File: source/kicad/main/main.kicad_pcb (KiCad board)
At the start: 4 copper layers, 50 x 50 mm, 108 parts

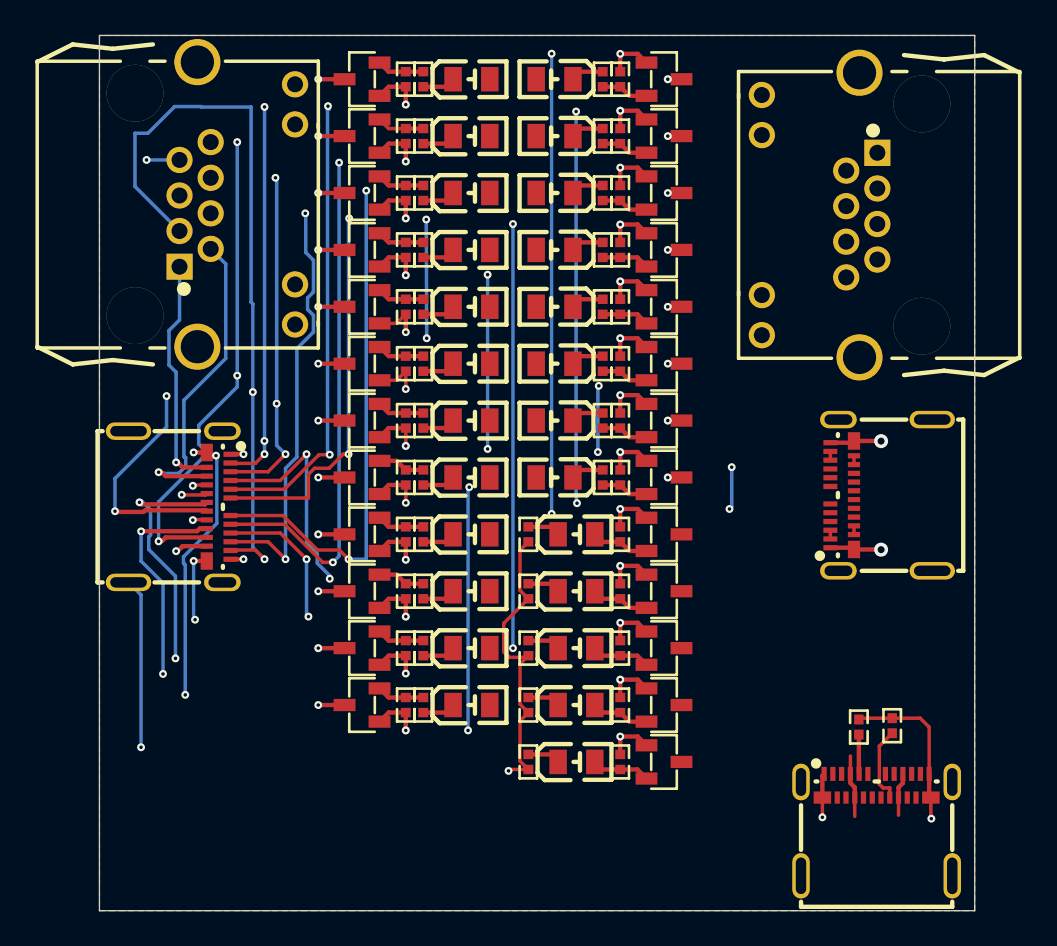
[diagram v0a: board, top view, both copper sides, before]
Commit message: bugfix/1.0.0 fixes (#3)
* Bugfixes 1.0.0; WIP; Not exported yet.

- Fixed USB-C PD resistors
- Improved part-picking
- Fixed LedIndicator (wrong PowerSwitch usage)
- Reduced LED brightness

* Fix footprints/3dmodels

* Place labels
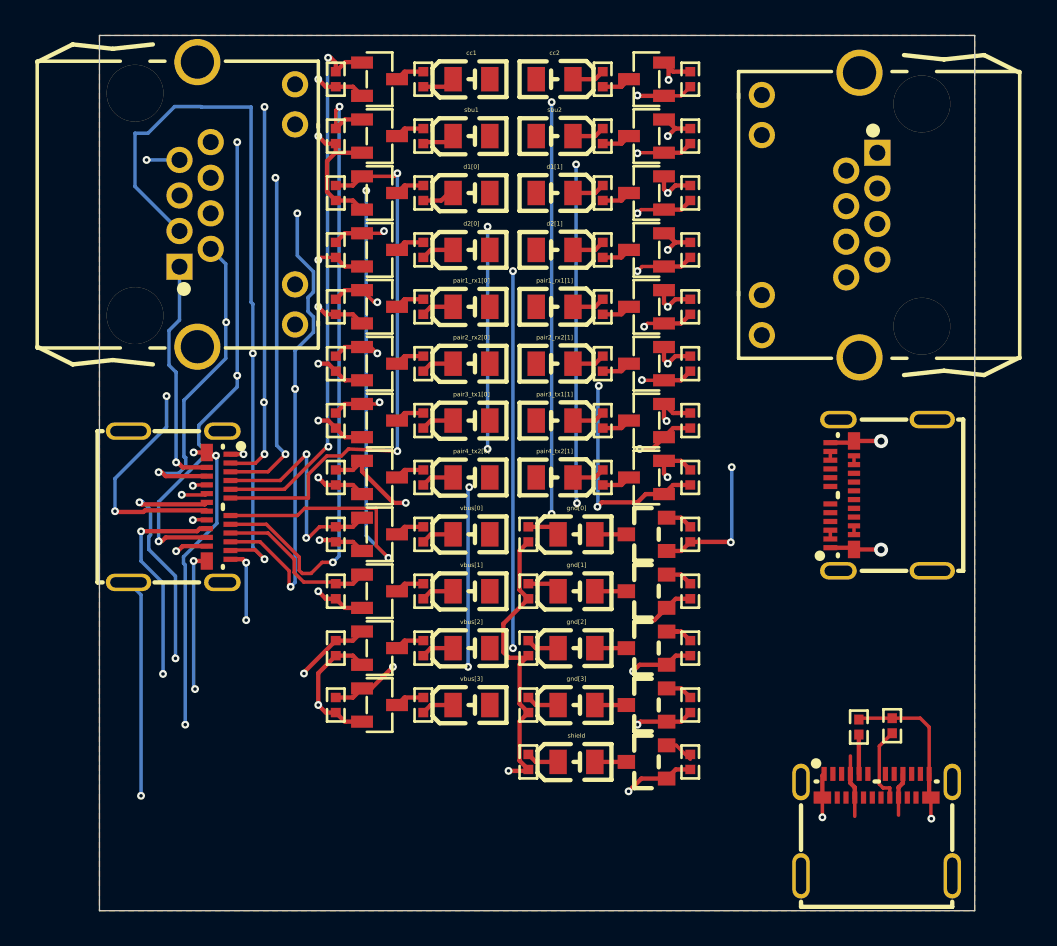
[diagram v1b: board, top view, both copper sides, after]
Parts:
- removed tester.cc1.indicator.led.current_limiting_resistor[Resistor:300Ω], tester.cc2.indicator.led.current_limiting_resistor[Resistor:300Ω], tester.d1[0].indicator.led.current_limiting_resistor[Resistor:300Ω], tester.d1[1].indicator.led.current_limiting_resistor[Resistor:300Ω], tester.d2[0].indicator.led.current_limiting_resistor[Resistor:300Ω], tester.d2[1].indicator.led.current_limiting_resistor[Resistor:300Ω], tester.gnd[0].indicator.led.current_limiting_resistor[Resistor:300Ω], tester.gnd[1].indicator.led.current_limiting_resistor[Resistor:300Ω], tester.gnd[2].indicator.led.current_limiting_resistor[Resistor:300Ω], tester.gnd[3].indicator.led.current_limiting_resistor[Resistor:300Ω], tester.pair1_rx1[0].indicator.led.current_limiting_resistor[Resistor:300Ω], tester.pair1_rx1[1].indicator.led.current_limiting_resistor[Resistor:300Ω], tester.pair2_rx2[0].indicator.led.current_limiting_resistor[Resistor:300Ω], tester.pair2_rx2[1].indicator.led.current_limiting_resistor[Resistor:300Ω], tester.pair3_tx1[0].indicator.led.current_limiting_resistor[Resistor:300Ω], tester.pair3_tx1[1].indicator.led.current_limiting_resistor[Resistor:300Ω], tester.pair4_tx2[0].indicator.led.current_limiting_resistor[Resistor:300Ω], tester.pair4_tx2[1].indicator.led.current_limiting_resistor[Resistor:300Ω], tester.sbu1.indicator.led.current_limiting_resistor[Resistor:300Ω], tester.sbu2.indicator.led.current_limiting_resistor[Resistor:300Ω], tester.shield.indicator.led.current_limiting_resistor[Resistor:300Ω], tester.vbus[0].indicator.led.current_limiting_resistor[Resistor:300Ω], tester.vbus[1].indicator.led.current_limiting_resistor[Resistor:300Ω], tester.vbus[2].indicator.led.current_limiting_resistor[Resistor:300Ω], tester.vbus[3].indicator.led.current_limiting_resistor[Resistor:300Ω]: 300Ω, lcsc:R0402
- removed the tester.gnd[0].indicator.power_switch.mosfet[MOSFET:Q] at (32.2, 28.5)
- removed the tester.gnd[1].indicator.power_switch.mosfet[MOSFET:Q] at (32.2, 31.8)
- removed the tester.gnd[2].indicator.power_switch.mosfet[MOSFET:Q] at (32.2, 35.0)
- removed the tester.gnd[3].indicator.power_switch.mosfet[MOSFET:Q] at (32.2, 38.2)
- removed the tester.shield.indicator.power_switch.mosfet[MOSFET:Q] at (32.2, 41.5)
- added tester.cc1.indicator.led.current_limiting_resistor[Resistor:1KΩ]: 1KΩ, lcsc:R0402, F.Cu at (18.5, 2.50)
- added tester.cc2.indicator.led.current_limiting_resistor[Resistor:1KΩ]: 1KΩ, lcsc:R0402, F.Cu at (28.8, 2.50)
- added tester.d1[0].indicator.led.current_limiting_resistor[Resistor:1KΩ]: 1KΩ, lcsc:R0402, F.Cu at (18.5, 9.00)
- added tester.d1[1].indicator.led.current_limiting_resistor[Resistor:1KΩ]: 1KΩ, lcsc:R0402, F.Cu at (28.8, 9.00)
- added tester.d2[0].indicator.led.current_limiting_resistor[Resistor:1KΩ]: 1KΩ, lcsc:R0402, F.Cu at (18.5, 12.2)
- added tester.d2[1].indicator.led.current_limiting_resistor[Resistor:1KΩ]: 1KΩ, lcsc:R0402, F.Cu at (28.8, 12.2)
- added tester.gnd[0].indicator.led.current_limiting_resistor[Resistor:1KΩ]: 1KΩ, lcsc:R0402, F.Cu at (24.5, 28.5)
- added tester.gnd[0].indicator.power_switch.mosfet[MOSFET:Q]: Q, lcsc:SOT-23_L2.9-W1.3-P1.90-LS2.4-BR, F.Cu at (31.2, 28.5)
- added tester.gnd[1].indicator.led.current_limiting_resistor[Resistor:1KΩ]: 1KΩ, lcsc:R0402, F.Cu at (24.5, 31.8)
- added tester.gnd[1].indicator.power_switch.mosfet[MOSFET:Q]: Q, lcsc:SOT-23_L2.9-W1.3-P1.90-LS2.4-BR, F.Cu at (31.2, 31.8)
- added tester.gnd[2].indicator.led.current_limiting_resistor[Resistor:1KΩ]: 1KΩ, lcsc:R0402, F.Cu at (24.5, 35.0)
- added tester.gnd[2].indicator.power_switch.mosfet[MOSFET:Q]: Q, lcsc:SOT-23_L2.9-W1.3-P1.90-LS2.4-BR, F.Cu at (31.2, 35.0)
- added tester.gnd[3].indicator.led.current_limiting_resistor[Resistor:1KΩ]: 1KΩ, lcsc:R0402, F.Cu at (24.5, 38.2)
- added tester.gnd[3].indicator.power_switch.mosfet[MOSFET:Q]: Q, lcsc:SOT-23_L2.9-W1.3-P1.90-LS2.4-BR, F.Cu at (31.2, 38.2)
- added tester.pair1_rx1[0].indicator.led.current_limiting_resistor[Resistor:1KΩ]: 1KΩ, lcsc:R0402, F.Cu at (18.5, 15.5)
- added tester.pair1_rx1[1].indicator.led.current_limiting_resistor[Resistor:1KΩ]: 1KΩ, lcsc:R0402, F.Cu at (28.8, 15.5)
- added tester.pair2_rx2[0].indicator.led.current_limiting_resistor[Resistor:1KΩ]: 1KΩ, lcsc:R0402, F.Cu at (18.5, 18.8)
- added tester.pair2_rx2[1].indicator.led.current_limiting_resistor[Resistor:1KΩ]: 1KΩ, lcsc:R0402, F.Cu at (28.8, 18.8)
- added tester.pair3_tx1[0].indicator.led.current_limiting_resistor[Resistor:1KΩ]: 1KΩ, lcsc:R0402, F.Cu at (18.5, 22.0)
- added tester.pair3_tx1[1].indicator.led.current_limiting_resistor[Resistor:1KΩ]: 1KΩ, lcsc:R0402, F.Cu at (28.8, 22.0)
- added tester.pair4_tx2[0].indicator.led.current_limiting_resistor[Resistor:1KΩ]: 1KΩ, lcsc:R0402, F.Cu at (18.5, 25.2)
- added tester.pair4_tx2[1].indicator.led.current_limiting_resistor[Resistor:1KΩ]: 1KΩ, lcsc:R0402, F.Cu at (28.8, 25.2)
- added tester.sbu1.indicator.led.current_limiting_resistor[Resistor:1KΩ]: 1KΩ, lcsc:R0402, F.Cu at (18.5, 5.75)
- added tester.sbu2.indicator.led.current_limiting_resistor[Resistor:1KΩ]: 1KΩ, lcsc:R0402, F.Cu at (28.8, 5.75)
- added tester.shield.indicator.led.current_limiting_resistor[Resistor:1KΩ]: 1KΩ, lcsc:R0402, F.Cu at (24.5, 41.5)
- added tester.shield.indicator.power_switch.mosfet[MOSFET:Q]: Q, lcsc:SOT-23_L2.9-W1.3-P1.90-LS2.4-BR, F.Cu at (31.2, 41.5)
- added tester.vbus[0].indicator.led.current_limiting_resistor[Resistor:1KΩ]: 1KΩ, lcsc:R0402, F.Cu at (18.5, 28.5)
- added tester.vbus[1].indicator.led.current_limiting_resistor[Resistor:1KΩ]: 1KΩ, lcsc:R0402, F.Cu at (18.5, 31.8)
- added tester.vbus[2].indicator.led.current_limiting_resistor[Resistor:1KΩ]: 1KΩ, lcsc:R0402, F.Cu at (18.5, 35.0)
- added tester.vbus[3].indicator.led.current_limiting_resistor[Resistor:1KΩ]: 1KΩ, lcsc:R0402, F.Cu at (18.5, 38.2)
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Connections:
- net psu.configuration_resistors[0][Resistor:5.0KΩ]-psu.usb[USB_C_Receptacle:x] renamed psu.usb[USB_C_Receptacle:x]-psu.configuration_resistors[0][Resistor:5.0KΩ]
- net tester.cc1[PairTester:virt]:4-tester.cc1.indicator[LEDIndicator:virt]-tester.cc1.indicator.power_swi renamed tester.cc1.indicator[LEDIndicator:virt]-tester.cc1.indicator.power_switch[PowerSwitch:virt]-tester.c
- net tester.cc2[PairTester:virt]:4-tester.cc2.indicator.power_switch[PowerSwitch:virt]-tester.cc2.indicat renamed tester.cc2.indicator.power_switch[PowerSwitch:virt]-tester.cc2.indicator[LEDIndicator:virt]-tester.c
- net tester.d1[0].indicator.power_switch[PowerSwitch:virt]-tester.d1[0][PairTester:virt]:4-tester.d1[0].i renamed tester.d1[0].indicator[LEDIndicator:virt]-tester.d1[0].indicator.power_switch[PowerSwitch:virt]-test
- net tester.d1[1].indicator.power_switch[PowerSwitch:virt]-tester.d1[1].indicator[LEDIndicator:virt]-test renamed tester.d1[1].indicator.power_switch[PowerSwitch:virt]-tester.d1[1][PairTester:virt]:4-tester.d1[1].i
- net tester.d2[1].indicator.power_switch[PowerSwitch:virt]-tester.d2[1][PairTester:virt]:4-tester.d2[1].i renamed tester.d2[1][PairTester:virt]:4-tester.d2[1].indicator[LEDIndicator:virt]-tester.d2[1].indicator.pow
- net tester.gnd[0].indicator[LEDIndicator:virt]-tester.gnd[0][PairTester:virt]:4-tester.gnd[0].indicator. renamed tester.gnd[0].indicator.power_switch[PowerSwitch:virt]-tester.gnd[0].indicator[LEDIndicator:virt]-te
- net tester.gnd[1].indicator[LEDIndicator:virt]-tester.gnd[1][PairTester:virt]:4-tester.gnd[1].indicator. renamed tester.gnd[1][PairTester:virt]:4-tester.gnd[1].indicator.power_switch[PowerSwitch:virt]-tester.gnd[1
- net tester.gnd[2].indicator[LEDIndicator:virt]-tester.gnd[2][PairTester:virt]:4-tester.gnd[2].indicator. renamed tester.gnd[2][PairTester:virt]:4-tester.gnd[2].indicator[LEDIndicator:virt]-tester.gnd[2].indicator.
- net tester.pair1_rx1[0].indicator[LEDIndicator:virt]-tester.pair1_rx1[0][PairTester:virt]:4-tester.pair1 renamed tester.pair1_rx1[0][PairTester:virt]:4-tester.pair1_rx1[0].indicator.power_switch[PowerSwitch:virt]-
- net tester.pair1_rx1[1][PairTester:virt]:4-tester.pair1_rx1[1].indicator.power_switch[PowerSwitch:virt]- renamed tester.pair1_rx1[1][PairTester:virt]:4-tester.pair1_rx1[1].indicator[LEDIndicator:virt]-tester.pair1
- net tester.pair2_rx2[0].indicator.power_switch[PowerSwitch:virt]-tester.pair2_rx2[0].indicator[LEDIndica renamed tester.pair2_rx2[0].indicator[LEDIndicator:virt]-tester.pair2_rx2[0][PairTester:virt]:4-tester.pair2
- net tester.pair2_rx2[1].indicator[LEDIndicator:virt]-tester.pair2_rx2[1][PairTester:virt]:4-tester.pair2 renamed tester.pair2_rx2[1].indicator.power_switch[PowerSwitch:virt]-tester.pair2_rx2[1].indicator[LEDIndica
- net tester.pair3_tx1[0].indicator[LEDIndicator:virt]-tester.pair3_tx1[0][PairTester:virt]:4-tester.pair3 renamed tester.pair3_tx1[0].indicator.power_switch[PowerSwitch:virt]-tester.pair3_tx1[0][PairTester:virt]:4-
- net tester.pair4_tx2[0].indicator.power_switch[PowerSwitch:virt]-tester.pair4_tx2[0].indicator[LEDIndica renamed tester.pair4_tx2[0].indicator[LEDIndicator:virt]-tester.pair4_tx2[0].indicator.power_switch[PowerSwi
- net tester.pair4_tx2[1][PairTester:virt]:4-tester.pair4_tx2[1].indicator[LEDIndicator:virt]-tester.pair4 renamed tester.pair4_tx2[1].indicator[LEDIndicator:virt]-tester.pair4_tx2[1].indicator.power_switch[PowerSwi
- net tester.sbu2[PairTester:virt]:4-tester.sbu2.indicator.power_switch[PowerSwitch:virt]-tester.sbu2.indi renamed tester.sbu2.indicator.power_switch[PowerSwitch:virt]-tester.sbu2[PairTester:virt]:4-tester.sbu2.indi
- net tester.shield[PairTester:virt]:4-tester.shield.indicator[LEDIndicator:virt]-tester.shield.indicator. renamed tester.shield.indicator.power_switch[PowerSwitch:virt]-tester.shield.indicator[LEDIndicator:virt]-te
- net tester.vbus[0].indicator[LEDIndicator:virt]-tester.vbus[0][PairTester:virt]:4-tester.vbus[0].indicat renamed tester.vbus[0][PairTester:virt]:4-tester.vbus[0].indicator[LEDIndicator:virt]-tester.vbus[0].indicat
- net tester.vbus[1].indicator.power_switch[PowerSwitch:virt]-tester.vbus[1][PairTester:virt]:4-tester.vbu renamed tester.vbus[1][PairTester:virt]:4-tester.vbus[1].indicator.power_switch[PowerSwitch:virt]-tester.vbu
- psu.configuration_resistors[0][Resistor:5.0KΩ] pad 2: tester.pair1_rx1[1][PairTester:virt]:2-tester.cc1[PairTester:virt]:2-tester.gnd[0].indicator.power_s -> tester.vbus[1].indicator[LEDIndicator:virt]:3-tester.shield.indicator[LEDIndicator:virt]:3-tester.gn
- psu.configuration_resistors[1][Resistor:5.0KΩ] pad 2: tester.pair1_rx1[1][PairTester:virt]:2-tester.cc1[PairTester:virt]:2-tester.gnd[0].indicator.power_s -> tester.vbus[1].indicator[LEDIndicator:virt]:3-tester.shield.indicator[LEDIndicator:virt]:3-tester.gn
- psu.usb[USB_C_Receptacle:x] pad A1: tester.pair1_rx1[1][PairTester:virt]:2-tester.cc1[PairTester:virt]:2-tester.gnd[0].indicator.power_s -> tester.vbus[1].indicator[LEDIndicator:virt]:3-tester.shield.indicator[LEDIndicator:virt]:3-tester.gn
- psu.usb[USB_C_Receptacle:x] pad A12: tester.pair1_rx1[1][PairTester:virt]:2-tester.cc1[PairTester:virt]:2-tester.gnd[0].indicator.power_s -> tester.vbus[1].indicator[LEDIndicator:virt]:3-tester.shield.indicator[LEDIndicator:virt]:3-tester.gn
- psu.usb[USB_C_Receptacle:x] pad A4: tester.d1[1].indicator.power_switch[PowerSwitch:virt]:4-tester.pair1_rx1[0].indicator.power_switch[P -> tester.pair1_rx1[1].indicator.led[PoweredLED:virt]-tester.d2[1].indicator.power_switch[PowerSwitch:v
- psu.usb[USB_C_Receptacle:x] pad A9: tester.d1[1].indicator.power_switch[PowerSwitch:virt]:4-tester.pair1_rx1[0].indicator.power_switch[P -> tester.pair1_rx1[1].indicator.led[PoweredLED:virt]-tester.d2[1].indicator.power_switch[PowerSwitch:v
- psu.usb[USB_C_Receptacle:x] pad B1: tester.pair1_rx1[1][PairTester:virt]:2-tester.cc1[PairTester:virt]:2-tester.gnd[0].indicator.power_s -> tester.vbus[1].indicator[LEDIndicator:virt]:3-tester.shield.indicator[LEDIndicator:virt]:3-tester.gn
- psu.usb[USB_C_Receptacle:x] pad B12: tester.pair1_rx1[1][PairTester:virt]:2-tester.cc1[PairTester:virt]:2-tester.gnd[0].indicator.power_s -> tester.vbus[1].indicator[LEDIndicator:virt]:3-tester.shield.indicator[LEDIndicator:virt]:3-tester.gn
- psu.usb[USB_C_Receptacle:x] pad B4: tester.d1[1].indicator.power_switch[PowerSwitch:virt]:4-tester.pair1_rx1[0].indicator.power_switch[P -> tester.pair1_rx1[1].indicator.led[PoweredLED:virt]-tester.d2[1].indicator.power_switch[PowerSwitch:v
- psu.usb[USB_C_Receptacle:x] pad B9: tester.d1[1].indicator.power_switch[PowerSwitch:virt]:4-tester.pair1_rx1[0].indicator.power_switch[P -> tester.pair1_rx1[1].indicator.led[PoweredLED:virt]-tester.d2[1].indicator.power_switch[PowerSwitch:v
- tester.cc1.indicator.led.led[LED:D] pad 1: tester.d1[1].indicator.power_switch[PowerSwitch:virt]:4-tester.pair1_rx1[0].indicator.power_switch[P -> tester.pair1_rx1[1].indicator.led[PoweredLED:virt]-tester.d2[1].indicator.power_switch[PowerSwitch:v
- tester.cc1.indicator.led.led[LED:D] pad 2: tester.cc1.indicator.led.led[LED:D]-tester.cc1.indicator.led.current_limiting_resistor[Resistor:300Ω] -> tester.cc1.indicator.led.current_limiting_resistor[Resistor:1KΩ]-tester.cc1.indicator.led.led[LED:D]
- tester.cc1.indicator.power_switch.mosfet[MOSFET:Q] pad 2: tester.cc1.indicator.led[PoweredLED:virt]:2-tester.cc1.indicator.power_switch[PowerSwitch:virt]:3 -> tester.vbus[1].indicator[LEDIndicator:virt]:3-tester.shield.indicator[LEDIndicator:virt]:3-tester.gn
- tester.cc1.indicator.power_switch.mosfet[MOSFET:Q] pad 3: tester.pair1_rx1[1][PairTester:virt]:2-tester.cc1[PairTester:virt]:2-tester.gnd[0].indicator.power_s -> tester.cc1.indicator.power_switch[PowerSwitch:virt]:5-tester.cc1.indicator.led[PoweredLED:virt]:2
- tester.cc1.indicator.power_switch.pull_resistor[Resistor:100KΩ] pad 2: tester.cc1.indicator.led[PoweredLED:virt]:2-tester.cc1.indicator.power_switch[PowerSwitch:virt]:3 -> tester.vbus[1].indicator[LEDIndicator:virt]:3-tester.shield.indicator[LEDIndicator:virt]:3-tester.gn
- tester.cc2.indicator.led.led[LED:D] pad 1: tester.d1[1].indicator.power_switch[PowerSwitch:virt]:4-tester.pair1_rx1[0].indicator.power_switch[P -> tester.pair1_rx1[1].indicator.led[PoweredLED:virt]-tester.d2[1].indicator.power_switch[PowerSwitch:v
- tester.cc2.indicator.led.led[LED:D] pad 2: tester.cc2.indicator.led.current_limiting_resistor[Resistor:300Ω]-tester.cc2.indicator.led.led[LED:D] -> tester.cc2.indicator.led.led[LED:D]-tester.cc2.indicator.led.current_limiting_resistor[Resistor:1KΩ]
- tester.cc2.indicator.power_switch.mosfet[MOSFET:Q] pad 2: tester.cc2.indicator.power_switch[PowerSwitch:virt]:3-tester.cc2.indicator.led[PoweredLED:virt]:2 -> tester.vbus[1].indicator[LEDIndicator:virt]:3-tester.shield.indicator[LEDIndicator:virt]:3-tester.gn
- tester.cc2.indicator.power_switch.mosfet[MOSFET:Q] pad 3: tester.pair1_rx1[1][PairTester:virt]:2-tester.cc1[PairTester:virt]:2-tester.gnd[0].indicator.power_s -> tester.cc2.indicator.power_switch[PowerSwitch:virt]:5-tester.cc2.indicator.led[PoweredLED:virt]:2
- tester.cc2.indicator.power_switch.pull_resistor[Resistor:100KΩ] pad 2: tester.cc2.indicator.power_switch[PowerSwitch:virt]:3-tester.cc2.indicator.led[PoweredLED:virt]:2 -> tester.vbus[1].indicator[LEDIndicator:virt]:3-tester.shield.indicator[LEDIndicator:virt]:3-tester.gn
- tester.d1[0].indicator.led.led[LED:D] pad 1: tester.d1[1].indicator.power_switch[PowerSwitch:virt]:4-tester.pair1_rx1[0].indicator.power_switch[P -> tester.pair1_rx1[1].indicator.led[PoweredLED:virt]-tester.d2[1].indicator.power_switch[PowerSwitch:v
- tester.d1[0].indicator.led.led[LED:D] pad 2: tester.d1[0].indicator.led.led[LED:D]-tester.d1[0].indicator.led.current_limiting_resistor[Resistor:300Ω] -> tester.d1[0].indicator.led.current_limiting_resistor[Resistor:1KΩ]-tester.d1[0].indicator.led.led[LED:D]
- tester.d1[0].indicator.power_switch.mosfet[MOSFET:Q] pad 2: tester.d1[0].indicator.led[PoweredLED:virt]:2-tester.d1[0].indicator.power_switch[PowerSwitch:virt]: -> tester.vbus[1].indicator[LEDIndicator:virt]:3-tester.shield.indicator[LEDIndicator:virt]:3-tester.gn
- tester.d1[0].indicator.power_switch.mosfet[MOSFET:Q] pad 3: tester.pair1_rx1[1][PairTester:virt]:2-tester.cc1[PairTester:virt]:2-tester.gnd[0].indicator.power_s -> tester.d1[0].indicator.led[PoweredLED:virt]:2-tester.d1[0].indicator.power_switch[PowerSwitch:virt]:
- tester.d1[0].indicator.power_switch.pull_resistor[Resistor:100KΩ] pad 2: tester.d1[0].indicator.led[PoweredLED:virt]:2-tester.d1[0].indicator.power_switch[PowerSwitch:virt]: -> tester.vbus[1].indicator[LEDIndicator:virt]:3-tester.shield.indicator[LEDIndicator:virt]:3-tester.gn
- tester.d1[1].indicator.led.led[LED:D] pad 1: tester.d1[1].indicator.power_switch[PowerSwitch:virt]:4-tester.pair1_rx1[0].indicator.power_switch[P -> tester.pair1_rx1[1].indicator.led[PoweredLED:virt]-tester.d2[1].indicator.power_switch[PowerSwitch:v
- tester.d1[1].indicator.led.led[LED:D] pad 2: tester.d1[1].indicator.led.current_limiting_resistor[Resistor:300Ω]-tester.d1[1].indicator.led.led[LED:D] -> tester.d1[1].indicator.led.led[LED:D]-tester.d1[1].indicator.led.current_limiting_resistor[Resistor:1KΩ]
- tester.d1[1].indicator.power_switch.mosfet[MOSFET:Q] pad 2: tester.d1[1].indicator.led[PoweredLED:virt]:2-tester.d1[1].indicator.power_switch[PowerSwitch:virt]: -> tester.vbus[1].indicator[LEDIndicator:virt]:3-tester.shield.indicator[LEDIndicator:virt]:3-tester.gn
- tester.d1[1].indicator.power_switch.mosfet[MOSFET:Q] pad 3: tester.pair1_rx1[1][PairTester:virt]:2-tester.cc1[PairTester:virt]:2-tester.gnd[0].indicator.power_s -> tester.d1[1].indicator.power_switch[PowerSwitch:virt]:5-tester.d1[1].indicator.led[PoweredLED:virt]:
- tester.d1[1].indicator.power_switch.pull_resistor[Resistor:100KΩ] pad 2: tester.d1[1].indicator.led[PoweredLED:virt]:2-tester.d1[1].indicator.power_switch[PowerSwitch:virt]: -> tester.vbus[1].indicator[LEDIndicator:virt]:3-tester.shield.indicator[LEDIndicator:virt]:3-tester.gn
- tester.d2[0].indicator.led.led[LED:D] pad 1: tester.d1[1].indicator.power_switch[PowerSwitch:virt]:4-tester.pair1_rx1[0].indicator.power_switch[P -> tester.pair1_rx1[1].indicator.led[PoweredLED:virt]-tester.d2[1].indicator.power_switch[PowerSwitch:v
- tester.d2[0].indicator.led.led[LED:D] pad 2: tester.d2[0].indicator.led.current_limiting_resistor[Resistor:300Ω]-tester.d2[0].indicator.led.led[LED:D] -> tester.d2[0].indicator.led.current_limiting_resistor[Resistor:1KΩ]-tester.d2[0].indicator.led.led[LED:D]
- tester.d2[0].indicator.power_switch.mosfet[MOSFET:Q] pad 2: tester.d2[0].indicator.led[PoweredLED:virt]:2-tester.d2[0].indicator.power_switch[PowerSwitch:virt]: -> tester.vbus[1].indicator[LEDIndicator:virt]:3-tester.shield.indicator[LEDIndicator:virt]:3-tester.gn
- tester.d2[0].indicator.power_switch.mosfet[MOSFET:Q] pad 3: tester.pair1_rx1[1][PairTester:virt]:2-tester.cc1[PairTester:virt]:2-tester.gnd[0].indicator.power_s -> tester.d2[0].indicator.power_switch[PowerSwitch:virt]:5-tester.d2[0].indicator.led[PoweredLED:virt]:
- tester.d2[0].indicator.power_switch.pull_resistor[Resistor:100KΩ] pad 2: tester.d2[0].indicator.led[PoweredLED:virt]:2-tester.d2[0].indicator.power_switch[PowerSwitch:virt]: -> tester.vbus[1].indicator[LEDIndicator:virt]:3-tester.shield.indicator[LEDIndicator:virt]:3-tester.gn
- tester.d2[1].indicator.led.led[LED:D] pad 1: tester.d1[1].indicator.power_switch[PowerSwitch:virt]:4-tester.pair1_rx1[0].indicator.power_switch[P -> tester.pair1_rx1[1].indicator.led[PoweredLED:virt]-tester.d2[1].indicator.power_switch[PowerSwitch:v
- tester.d2[1].indicator.led.led[LED:D] pad 2: tester.d2[1].indicator.led.current_limiting_resistor[Resistor:300Ω]-tester.d2[1].indicator.led.led[LED:D] -> tester.d2[1].indicator.led.current_limiting_resistor[Resistor:1KΩ]-tester.d2[1].indicator.led.led[LED:D]
- tester.d2[1].indicator.power_switch.mosfet[MOSFET:Q] pad 2: tester.d2[1].indicator.led[PoweredLED:virt]:2-tester.d2[1].indicator.power_switch[PowerSwitch:virt]: -> tester.vbus[1].indicator[LEDIndicator:virt]:3-tester.shield.indicator[LEDIndicator:virt]:3-tester.gn
- tester.d2[1].indicator.power_switch.mosfet[MOSFET:Q] pad 3: tester.pair1_rx1[1][PairTester:virt]:2-tester.cc1[PairTester:virt]:2-tester.gnd[0].indicator.power_s -> tester.d2[1].indicator.power_switch[PowerSwitch:virt]:5-tester.d2[1].indicator.led[PoweredLED:virt]:
- tester.d2[1].indicator.power_switch.pull_resistor[Resistor:100KΩ] pad 2: tester.d2[1].indicator.led[PoweredLED:virt]:2-tester.d2[1].indicator.power_switch[PowerSwitch:virt]: -> tester.vbus[1].indicator[LEDIndicator:virt]:3-tester.shield.indicator[LEDIndicator:virt]:3-tester.gn
- tester.gnd[0].indicator.led.led[LED:D] pad 1: tester.gnd[0].indicator.led[PoweredLED:virt]-tester.gnd[0].indicator.power_switch[PowerSwitch:virt]: -> tester.gnd[0].indicator.power_switch[PowerSwitch:virt]:4-tester.gnd[0].indicator.led[PoweredLED:virt
- tester.gnd[0].indicator.led.led[LED:D] pad 2: tester.gnd[0].indicator.led.led[LED:D]-tester.gnd[0].indicator.led.current_limiting_resistor[Resistor:300Ω] -> tester.gnd[0].indicator.led.led[LED:D]-tester.gnd[0].indicator.led.current_limiting_resistor[Resistor:1KΩ]
- tester.gnd[0].indicator.power_switch.pull_resistor[Resistor:100KΩ] pad 2: tester.gnd[0].indicator.led[PoweredLED:virt]-tester.gnd[0].indicator.power_switch[PowerSwitch:virt]: -> tester.pair1_rx1[1].indicator.led[PoweredLED:virt]-tester.d2[1].indicator.power_switch[PowerSwitch:v
- tester.gnd[1].indicator.led.led[LED:D] pad 1: tester.gnd[1].indicator.power_switch[PowerSwitch:virt]:2-tester.gnd[1].indicator.led[PoweredLED:virt -> tester.gnd[1].indicator.power_switch[PowerSwitch:virt]:4-tester.gnd[1].indicator.led[PoweredLED:virt
- tester.gnd[1].indicator.led.led[LED:D] pad 2: tester.gnd[1].indicator.led.current_limiting_resistor[Resistor:300Ω]-tester.gnd[1].indicator.led.led[LED:D] -> tester.gnd[1].indicator.led.led[LED:D]-tester.gnd[1].indicator.led.current_limiting_resistor[Resistor:1KΩ]
- tester.gnd[1].indicator.power_switch.pull_resistor[Resistor:100KΩ] pad 2: tester.gnd[1].indicator.power_switch[PowerSwitch:virt]:2-tester.gnd[1].indicator.led[PoweredLED:virt -> tester.pair1_rx1[1].indicator.led[PoweredLED:virt]-tester.d2[1].indicator.power_switch[PowerSwitch:v
- tester.gnd[2].indicator.led.led[LED:D] pad 2: tester.gnd[2].indicator.led.current_limiting_resistor[Resistor:300Ω]-tester.gnd[2].indicator.led.led[LED:D] -> tester.gnd[2].indicator.led.led[LED:D]-tester.gnd[2].indicator.led.current_limiting_resistor[Resistor:1KΩ]
- tester.gnd[2].indicator.power_switch.pull_resistor[Resistor:100KΩ] pad 2: tester.gnd[2].indicator.led[PoweredLED:virt]-tester.gnd[2].indicator.power_switch[PowerSwitch:virt]: -> tester.pair1_rx1[1].indicator.led[PoweredLED:virt]-tester.d2[1].indicator.power_switch[PowerSwitch:v
- tester.gnd[3].indicator.led.led[LED:D] pad 2: tester.gnd[3].indicator.led.led[LED:D]-tester.gnd[3].indicator.led.current_limiting_resistor[Resistor:300Ω] -> tester.gnd[3].indicator.led.led[LED:D]-tester.gnd[3].indicator.led.current_limiting_resistor[Resistor:1KΩ]
- tester.gnd[3].indicator.power_switch.pull_resistor[Resistor:100KΩ] pad 2: tester.gnd[3].indicator.led[PoweredLED:virt]-tester.gnd[3].indicator.power_switch[PowerSwitch:virt]: -> tester.pair1_rx1[1].indicator.led[PoweredLED:virt]-tester.d2[1].indicator.power_switch[PowerSwitch:v
- tester.pair1_rx1[0].indicator.led.led[LED:D] pad 1: tester.d1[1].indicator.power_switch[PowerSwitch:virt]:4-tester.pair1_rx1[0].indicator.power_switch[P -> tester.pair1_rx1[1].indicator.led[PoweredLED:virt]-tester.d2[1].indicator.power_switch[PowerSwitch:v
- tester.pair1_rx1[0].indicator.led.led[LED:D] pad 2: tester.pair1_rx1[0].indicator.led.led[LED:D]-tester.pair1_rx1[0].indicator.led.current_limiting_resistor[Resistor:300Ω] -> tester.pair1_rx1[0].indicator.led.led[LED:D]-tester.pair1_rx1[0].indicator.led.current_limiting_resistor[Resistor:1KΩ]
- tester.pair1_rx1[0].indicator.power_switch.mosfet[MOSFET:Q] pad 2: tester.pair1_rx1[0].indicator.led[PoweredLED:virt]:2-tester.pair1_rx1[0].indicator.power_switch[Powe -> tester.vbus[1].indicator[LEDIndicator:virt]:3-tester.shield.indicator[LEDIndicator:virt]:3-tester.gn
- tester.pair1_rx1[0].indicator.power_switch.mosfet[MOSFET:Q] pad 3: tester.pair1_rx1[1][PairTester:virt]:2-tester.cc1[PairTester:virt]:2-tester.gnd[0].indicator.power_s -> tester.pair1_rx1[0].indicator.led[PoweredLED:virt]:2-tester.pair1_rx1[0].indicator.power_switch[Powe
- tester.pair1_rx1[0].indicator.power_switch.pull_resistor[Resistor:100KΩ] pad 2: tester.pair1_rx1[0].indicator.led[PoweredLED:virt]:2-tester.pair1_rx1[0].indicator.power_switch[Powe -> tester.vbus[1].indicator[LEDIndicator:virt]:3-tester.shield.indicator[LEDIndicator:virt]:3-tester.gn
- tester.pair1_rx1[1].indicator.led.led[LED:D] pad 1: tester.d1[1].indicator.power_switch[PowerSwitch:virt]:4-tester.pair1_rx1[0].indicator.power_switch[P -> tester.pair1_rx1[1].indicator.led[PoweredLED:virt]-tester.d2[1].indicator.power_switch[PowerSwitch:v
- tester.pair1_rx1[1].indicator.led.led[LED:D] pad 2: tester.pair1_rx1[1].indicator.led.led[LED:D]-tester.pair1_rx1[1].indicator.led.current_limiting_resistor[Resistor:300Ω] -> tester.pair1_rx1[1].indicator.led.current_limiting_resistor[Resistor:1KΩ]-tester.pair1_rx1[1].indicator.led.led[LED:D]
- tester.pair1_rx1[1].indicator.power_switch.mosfet[MOSFET:Q] pad 2: tester.pair1_rx1[1].indicator.led[PoweredLED:virt]:2-tester.pair1_rx1[1].indicator.power_switch[Powe -> tester.vbus[1].indicator[LEDIndicator:virt]:3-tester.shield.indicator[LEDIndicator:virt]:3-tester.gn
- tester.pair1_rx1[1].indicator.power_switch.mosfet[MOSFET:Q] pad 3: tester.pair1_rx1[1][PairTester:virt]:2-tester.cc1[PairTester:virt]:2-tester.gnd[0].indicator.power_s -> tester.pair1_rx1[1].indicator.power_switch[PowerSwitch:virt]:5-tester.pair1_rx1[1].indicator.led[Pow
- tester.pair1_rx1[1].indicator.power_switch.pull_resistor[Resistor:100KΩ] pad 2: tester.pair1_rx1[1].indicator.led[PoweredLED:virt]:2-tester.pair1_rx1[1].indicator.power_switch[Powe -> tester.vbus[1].indicator[LEDIndicator:virt]:3-tester.shield.indicator[LEDIndicator:virt]:3-tester.gn
- tester.pair2_rx2[0].indicator.led.led[LED:D] pad 1: tester.d1[1].indicator.power_switch[PowerSwitch:virt]:4-tester.pair1_rx1[0].indicator.power_switch[P -> tester.pair1_rx1[1].indicator.led[PoweredLED:virt]-tester.d2[1].indicator.power_switch[PowerSwitch:v
- tester.pair2_rx2[0].indicator.led.led[LED:D] pad 2: tester.pair2_rx2[0].indicator.led.current_limiting_resistor[Resistor:300Ω]-tester.pair2_rx2[0].indicator.led.led[LED:D] -> tester.pair2_rx2[0].indicator.led.led[LED:D]-tester.pair2_rx2[0].indicator.led.current_limiting_resistor[Resistor:1KΩ]
- tester.pair2_rx2[0].indicator.power_switch.mosfet[MOSFET:Q] pad 2: tester.pair2_rx2[0].indicator.led[PoweredLED:virt]:2-tester.pair2_rx2[0].indicator.power_switch[Powe -> tester.vbus[1].indicator[LEDIndicator:virt]:3-tester.shield.indicator[LEDIndicator:virt]:3-tester.gn
- tester.pair2_rx2[0].indicator.power_switch.mosfet[MOSFET:Q] pad 3: tester.pair1_rx1[1][PairTester:virt]:2-tester.cc1[PairTester:virt]:2-tester.gnd[0].indicator.power_s -> tester.pair2_rx2[0].indicator.power_switch[PowerSwitch:virt]:5-tester.pair2_rx2[0].indicator.led[Pow
- tester.pair2_rx2[0].indicator.power_switch.pull_resistor[Resistor:100KΩ] pad 2: tester.pair2_rx2[0].indicator.led[PoweredLED:virt]:2-tester.pair2_rx2[0].indicator.power_switch[Powe -> tester.vbus[1].indicator[LEDIndicator:virt]:3-tester.shield.indicator[LEDIndicator:virt]:3-tester.gn
- tester.pair2_rx2[1].indicator.led.led[LED:D] pad 1: tester.d1[1].indicator.power_switch[PowerSwitch:virt]:4-tester.pair1_rx1[0].indicator.power_switch[P -> tester.pair1_rx1[1].indicator.led[PoweredLED:virt]-tester.d2[1].indicator.power_switch[PowerSwitch:v
- tester.pair2_rx2[1].indicator.led.led[LED:D] pad 2: tester.pair2_rx2[1].indicator.led.led[LED:D]-tester.pair2_rx2[1].indicator.led.current_limiting_resistor[Resistor:300Ω] -> tester.pair2_rx2[1].indicator.led.current_limiting_resistor[Resistor:1KΩ]-tester.pair2_rx2[1].indicator.led.led[LED:D]
- tester.pair2_rx2[1].indicator.power_switch.mosfet[MOSFET:Q] pad 2: tester.pair2_rx2[1].indicator.power_switch[PowerSwitch:virt]:3-tester.pair2_rx2[1].indicator.led[Pow -> tester.vbus[1].indicator[LEDIndicator:virt]:3-tester.shield.indicator[LEDIndicator:virt]:3-tester.gn
- tester.pair2_rx2[1].indicator.power_switch.mosfet[MOSFET:Q] pad 3: tester.pair1_rx1[1][PairTester:virt]:2-tester.cc1[PairTester:virt]:2-tester.gnd[0].indicator.power_s -> tester.pair2_rx2[1].indicator.power_switch[PowerSwitch:virt]:5-tester.pair2_rx2[1].indicator.led[Pow
- tester.pair2_rx2[1].indicator.power_switch.pull_resistor[Resistor:100KΩ] pad 2: tester.pair2_rx2[1].indicator.power_switch[PowerSwitch:virt]:3-tester.pair2_rx2[1].indicator.led[Pow -> tester.vbus[1].indicator[LEDIndicator:virt]:3-tester.shield.indicator[LEDIndicator:virt]:3-tester.gn
- tester.pair3_tx1[0].indicator.led.led[LED:D] pad 1: tester.d1[1].indicator.power_switch[PowerSwitch:virt]:4-tester.pair1_rx1[0].indicator.power_switch[P -> tester.pair1_rx1[1].indicator.led[PoweredLED:virt]-tester.d2[1].indicator.power_switch[PowerSwitch:v
- tester.pair3_tx1[0].indicator.led.led[LED:D] pad 2: tester.pair3_tx1[0].indicator.led.led[LED:D]-tester.pair3_tx1[0].indicator.led.current_limiting_resistor[Resistor:300Ω] -> tester.pair3_tx1[0].indicator.led.current_limiting_resistor[Resistor:1KΩ]-tester.pair3_tx1[0].indicator.led.led[LED:D]
- tester.pair3_tx1[0].indicator.power_switch.mosfet[MOSFET:Q] pad 2: tester.pair3_tx1[0].indicator.led[PoweredLED:virt]:2-tester.pair3_tx1[0].indicator.power_switch[Powe -> tester.vbus[1].indicator[LEDIndicator:virt]:3-tester.shield.indicator[LEDIndicator:virt]:3-tester.gn
- tester.pair3_tx1[0].indicator.power_switch.mosfet[MOSFET:Q] pad 3: tester.pair1_rx1[1][PairTester:virt]:2-tester.cc1[PairTester:virt]:2-tester.gnd[0].indicator.power_s -> tester.pair3_tx1[0].indicator.power_switch[PowerSwitch:virt]:5-tester.pair3_tx1[0].indicator.led[Pow
- tester.pair3_tx1[0].indicator.power_switch.pull_resistor[Resistor:100KΩ] pad 2: tester.pair3_tx1[0].indicator.led[PoweredLED:virt]:2-tester.pair3_tx1[0].indicator.power_switch[Powe -> tester.vbus[1].indicator[LEDIndicator:virt]:3-tester.shield.indicator[LEDIndicator:virt]:3-tester.gn
- tester.pair3_tx1[1].indicator.led.led[LED:D] pad 1: tester.d1[1].indicator.power_switch[PowerSwitch:virt]:4-tester.pair1_rx1[0].indicator.power_switch[P -> tester.pair1_rx1[1].indicator.led[PoweredLED:virt]-tester.d2[1].indicator.power_switch[PowerSwitch:v
- tester.pair3_tx1[1].indicator.led.led[LED:D] pad 2: tester.pair3_tx1[1].indicator.led.current_limiting_resistor[Resistor:300Ω]-tester.pair3_tx1[1].indicator.led.led[LED:D] -> tester.pair3_tx1[1].indicator.led.current_limiting_resistor[Resistor:1KΩ]-tester.pair3_tx1[1].indicator.led.led[LED:D]
- tester.pair3_tx1[1].indicator.power_switch.mosfet[MOSFET:Q] pad 2: tester.pair3_tx1[1].indicator.power_switch[PowerSwitch:virt]:3-tester.pair3_tx1[1].indicator.led[Pow -> tester.vbus[1].indicator[LEDIndicator:virt]:3-tester.shield.indicator[LEDIndicator:virt]:3-tester.gn
- tester.pair3_tx1[1].indicator.power_switch.mosfet[MOSFET:Q] pad 3: tester.pair1_rx1[1][PairTester:virt]:2-tester.cc1[PairTester:virt]:2-tester.gnd[0].indicator.power_s -> tester.pair3_tx1[1].indicator.power_switch[PowerSwitch:virt]:5-tester.pair3_tx1[1].indicator.led[Pow
- tester.pair3_tx1[1].indicator.power_switch.pull_resistor[Resistor:100KΩ] pad 2: tester.pair3_tx1[1].indicator.power_switch[PowerSwitch:virt]:3-tester.pair3_tx1[1].indicator.led[Pow -> tester.vbus[1].indicator[LEDIndicator:virt]:3-tester.shield.indicator[LEDIndicator:virt]:3-tester.gn
- tester.pair4_tx2[0].indicator.led.led[LED:D] pad 1: tester.d1[1].indicator.power_switch[PowerSwitch:virt]:4-tester.pair1_rx1[0].indicator.power_switch[P -> tester.pair1_rx1[1].indicator.led[PoweredLED:virt]-tester.d2[1].indicator.power_switch[PowerSwitch:v
- tester.pair4_tx2[0].indicator.led.led[LED:D] pad 2: tester.pair4_tx2[0].indicator.led.led[LED:D]-tester.pair4_tx2[0].indicator.led.current_limiting_resistor[Resistor:300Ω] -> tester.pair4_tx2[0].indicator.led.led[LED:D]-tester.pair4_tx2[0].indicator.led.current_limiting_resistor[Resistor:1KΩ]
- tester.pair4_tx2[0].indicator.power_switch.mosfet[MOSFET:Q] pad 2: tester.pair4_tx2[0].indicator.power_switch[PowerSwitch:virt]:3-tester.pair4_tx2[0].indicator.led[Pow -> tester.vbus[1].indicator[LEDIndicator:virt]:3-tester.shield.indicator[LEDIndicator:virt]:3-tester.gn
- tester.pair4_tx2[0].indicator.power_switch.mosfet[MOSFET:Q] pad 3: tester.pair1_rx1[1][PairTester:virt]:2-tester.cc1[PairTester:virt]:2-tester.gnd[0].indicator.power_s -> tester.pair4_tx2[0].indicator.power_switch[PowerSwitch:virt]:5-tester.pair4_tx2[0].indicator.led[Pow
- tester.pair4_tx2[0].indicator.power_switch.pull_resistor[Resistor:100KΩ] pad 2: tester.pair4_tx2[0].indicator.power_switch[PowerSwitch:virt]:3-tester.pair4_tx2[0].indicator.led[Pow -> tester.vbus[1].indicator[LEDIndicator:virt]:3-tester.shield.indicator[LEDIndicator:virt]:3-tester.gn
- tester.pair4_tx2[1].indicator.led.led[LED:D] pad 1: tester.d1[1].indicator.power_switch[PowerSwitch:virt]:4-tester.pair1_rx1[0].indicator.power_switch[P -> tester.pair1_rx1[1].indicator.led[PoweredLED:virt]-tester.d2[1].indicator.power_switch[PowerSwitch:v
- tester.pair4_tx2[1].indicator.led.led[LED:D] pad 2: tester.pair4_tx2[1].indicator.led.current_limiting_resistor[Resistor:300Ω]-tester.pair4_tx2[1].indicator.led.led[LED:D] -> tester.pair4_tx2[1].indicator.led.led[LED:D]-tester.pair4_tx2[1].indicator.led.current_limiting_resistor[Resistor:1KΩ]
- tester.pair4_tx2[1].indicator.power_switch.mosfet[MOSFET:Q] pad 2: tester.pair4_tx2[1].indicator.power_switch[PowerSwitch:virt]:3-tester.pair4_tx2[1].indicator.led[Pow -> tester.vbus[1].indicator[LEDIndicator:virt]:3-tester.shield.indicator[LEDIndicator:virt]:3-tester.gn
- tester.pair4_tx2[1].indicator.power_switch.mosfet[MOSFET:Q] pad 3: tester.pair1_rx1[1][PairTester:virt]:2-tester.cc1[PairTester:virt]:2-tester.gnd[0].indicator.power_s -> tester.pair4_tx2[1].indicator.power_switch[PowerSwitch:virt]:5-tester.pair4_tx2[1].indicator.led[Pow
- tester.pair4_tx2[1].indicator.power_switch.pull_resistor[Resistor:100KΩ] pad 2: tester.pair4_tx2[1].indicator.power_switch[PowerSwitch:virt]:3-tester.pair4_tx2[1].indicator.led[Pow -> tester.vbus[1].indicator[LEDIndicator:virt]:3-tester.shield.indicator[LEDIndicator:virt]:3-tester.gn
- tester.rj45[0][RJ45_Receptacle:x] pad 1: tester.d1[1].indicator.power_switch[PowerSwitch:virt]:4-tester.pair1_rx1[0].indicator.power_switch[P -> tester.pair1_rx1[1].indicator.led[PoweredLED:virt]-tester.d2[1].indicator.power_switch[PowerSwitch:v
- tester.rj45[0][RJ45_Receptacle:x] pad 2: tester.d1[1].indicator.power_switch[PowerSwitch:virt]:4-tester.pair1_rx1[0].indicator.power_switch[P -> tester.pair1_rx1[1].indicator.led[PoweredLED:virt]-tester.d2[1].indicator.power_switch[PowerSwitch:v
- tester.rj45[0][RJ45_Receptacle:x] pad 3: tester.d1[1].indicator.power_switch[PowerSwitch:virt]:4-tester.pair1_rx1[0].indicator.power_switch[P -> tester.pair1_rx1[1].indicator.led[PoweredLED:virt]-tester.d2[1].indicator.power_switch[PowerSwitch:v
- tester.rj45[0][RJ45_Receptacle:x] pad 4: tester.d1[1].indicator.power_switch[PowerSwitch:virt]:4-tester.pair1_rx1[0].indicator.power_switch[P -> tester.pair1_rx1[1].indicator.led[PoweredLED:virt]-tester.d2[1].indicator.power_switch[PowerSwitch:v
- tester.rj45[0][RJ45_Receptacle:x] pad 5: tester.d1[1].indicator.power_switch[PowerSwitch:virt]:4-tester.pair1_rx1[0].indicator.power_switch[P -> tester.pair1_rx1[1].indicator.led[PoweredLED:virt]-tester.d2[1].indicator.power_switch[PowerSwitch:v
- tester.rj45[0][RJ45_Receptacle:x] pad 6: tester.d1[1].indicator.power_switch[PowerSwitch:virt]:4-tester.pair1_rx1[0].indicator.power_switch[P -> tester.pair1_rx1[1].indicator.led[PoweredLED:virt]-tester.d2[1].indicator.power_switch[PowerSwitch:v
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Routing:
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- added copper zone on F.Cu, net tester.pair1_rx1[1].indicator.led[PoweredLED:virt]-tester.d2[1].indicator.power_switch[PowerSwitch:v
- removed copper zone on F.Cu, net tester.d1[1].indicator.power_switch[PowerSwitch:virt]:4-tester.pair1_rx1[0].indicator.power_switch[P
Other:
- board text added: "USB-C CableTester v1.0.1 https://github.com/IoannisP-ITENG/CableTester"
- board text added: "cc1"
- board text added: "cc2"
- board text added: "d1[0]"
- board text added: "d1[1]"
- board text added: "d2[0]"
- board text added: "d2[1]"
- board text added: "gnd[0]"
- board text added: "gnd[1]"
- board text added: "gnd[2]"
- board text added: "gnd[3]"
- board text added: "pair1_rx1[0]"
- board text added: "pair1_rx1[1]"
- board text added: "pair2_rx2[0]"
- board text added: "pair2_rx2[1]"
- board text added: "pair3_tx1[0]"
- board text added: "pair3_tx1[1]"
- board text added: "pair4_tx2[0]"
- board text added: "pair4_tx2[1]"
- board text added: "sbu1"
- board text added: "sbu2"
- board text added: "shield"
- board text added: "vbus[0]"
- board text added: "vbus[1]"
- board text added: "vbus[2]"
- board text added: "vbus[3]"
- board text removed: "USB-C CableTester v1.0.0 https://github.com/IoannisP-ITENG/CableTester"
